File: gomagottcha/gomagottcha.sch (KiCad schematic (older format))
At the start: 88 parts, among them J1 USB_B_Micro, J2 Arduino_ICSP, SW1 SW_DIP_x01, U1 BM71BLES1FC2, U10 Buzzer_490-9647-1-ND, U11 IMU, U2 FT232RQ, U3 MCP7381, U4 ATMEGA1284P, U5 TPS2113APWR, U6 LCD_Tomagotcha, U7 MCP1700, U8 VMotor1670-1000-ND, U9 VMotor1670-1000-ND, Y1 Crystal

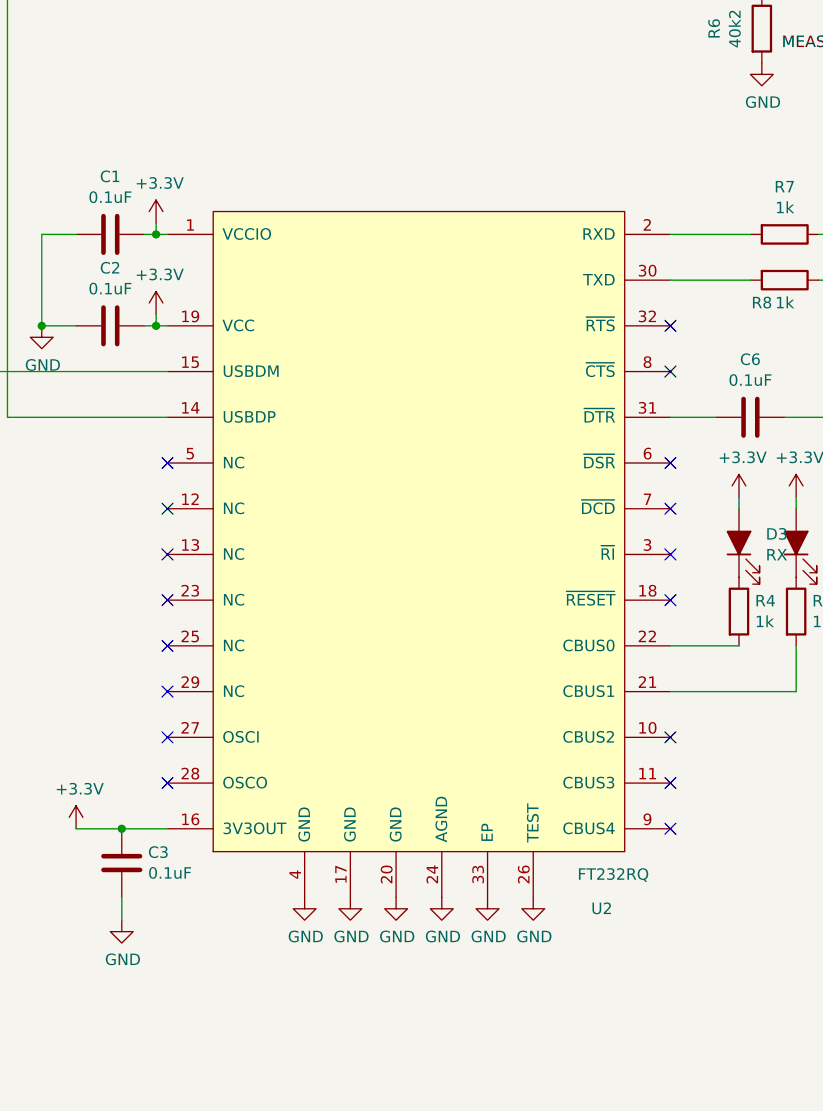
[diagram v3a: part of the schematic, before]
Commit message: Changed TCSP symbol from QFN to QFP
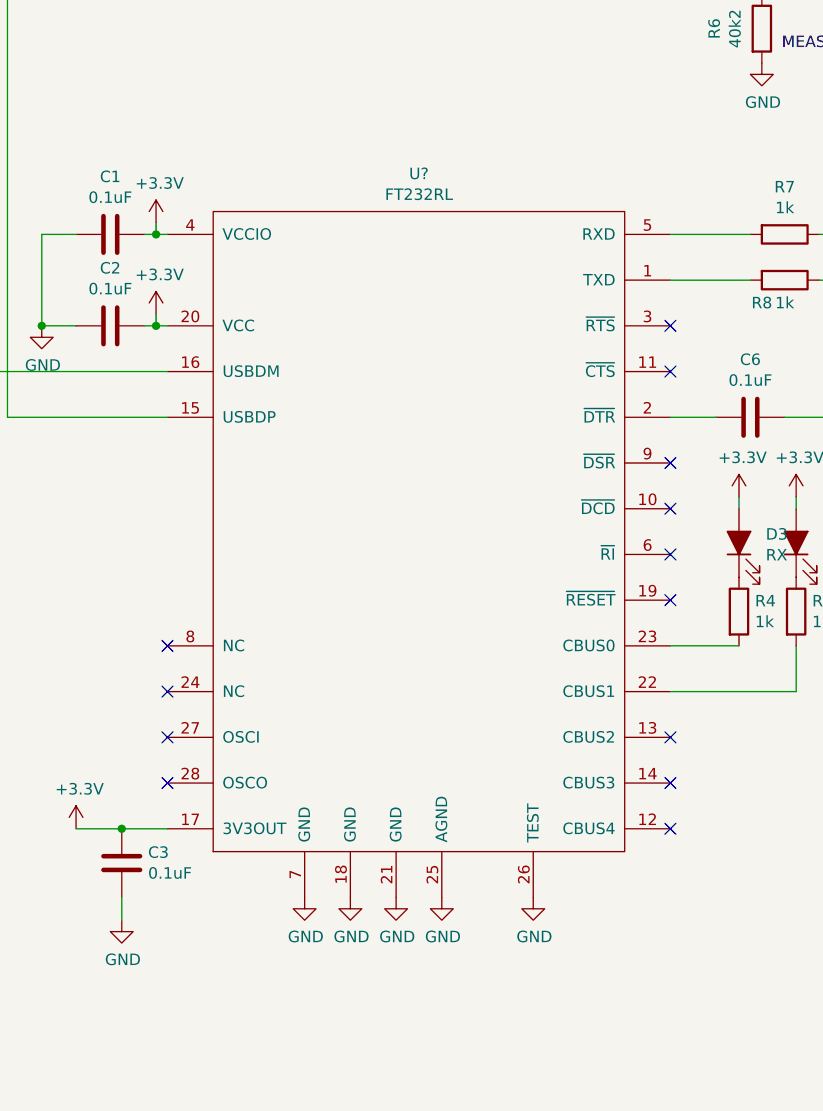
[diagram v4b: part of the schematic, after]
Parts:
- removed U2: FT232RQ, tama-footprints:QFN-32-1EP_5x5mm_P0.5mm_EP3.1x3.1mm_ThermalVias, symbol tama-sym:FT232RQ
- added U?: FT232RL, symbol tama-sym:FT232RL
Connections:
- net +3V3: now also U?.17 (3V3OUT), U?.20 (VCC), U?.4 (VCCIO)
- net GND: now also U?.18 (GND), U?.21 (GND), U?.25 (AGND), U?.26 (TEST), U?.7 (GND)
- net at J1.2 (D-): now also U?.16 (USBDM)
- net at J1.3 (D+): now also U?.15 (USBDP)
- net at R7.2: now also U?.5 (RXD)
- net at R9.2: now also U?.22 (CBUS1)
- net at R4.2: now also U?.23 (CBUS0)
- net at R8.2: now also U?.1 (TXD)
- net at C6.2: now also U?.2 (~DTR)
- no-connect marks 32 -> 28
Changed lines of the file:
@@
 	8200 1200 8200 1250
-$Comp
-L tama-sym:FT232RQ U2
-U 1 1 5CA563EE
-P 2750 5000
-F 0 "U2" H 3550 3350 50  0000 C CNN
-F 1 "FT232RQ" H 3600 3500 50  0000 C CNN
-F 2 "tama-footprints:QFN-32-1EP_5x5mm_P0.5mm_EP3.1x3.1mm_ThermalVias" H 2750 5950 50  0001 C CNN
-F 3 "" H 2750 5950 50  0001 C CNN
-	1    2750 5000
-	1    0    0    -1
-$EndComp
 $Comp
 L power:GND #PWR0106
@@
 	1100 4100 1250 4100
 Connection ~ 1100 4100
-NoConn ~ 1650 4700
-NoConn ~ 1650 4900
-NoConn ~ 1650 5100
-NoConn ~ 1650 5300
 NoConn ~ 1650 5500
 NoConn ~ 1650 5700
@@
 F 3 "" H 2850 6600 50  0001 C CNN
 	1    2850 6600
-	1    0    0    -1
-$EndComp
-$Comp
-L power:GND #PWR0116
-U 1 1 5CA6129E
-P 3050 6600
-F 0 "#PWR0116" H 3050 6350 50  0001 C CNN
-F 1 "GND" H 3055 6427 50  0000 C CNN
-F 2 "" H 3050 6600 50  0001 C CNN
-F 3 "" H 3050 6600 50  0001 C CNN
-	1    3050 6600
 	1    0    0    -1
 $EndComp
@@
 Wire Wire Line
 	3550 1300 3400 1300
+$Comp
+L tama-sym:FT232RL U?
+U 1 1 5CAFC7D3
+P 2750 5000
+F 0 "U?" H 2750 6565 50  0000 C CNN
+F 1 "FT232RL" H 2750 6474 50  0000 C CNN
+F 2 "" H 2750 5950 50  0001 C CNN
+F 3 "" H 2750 5950 50  0001 C CNN
+	1    2750 5000
+	1    0    0    -1
+$EndComp
 $EndSCHEMATC

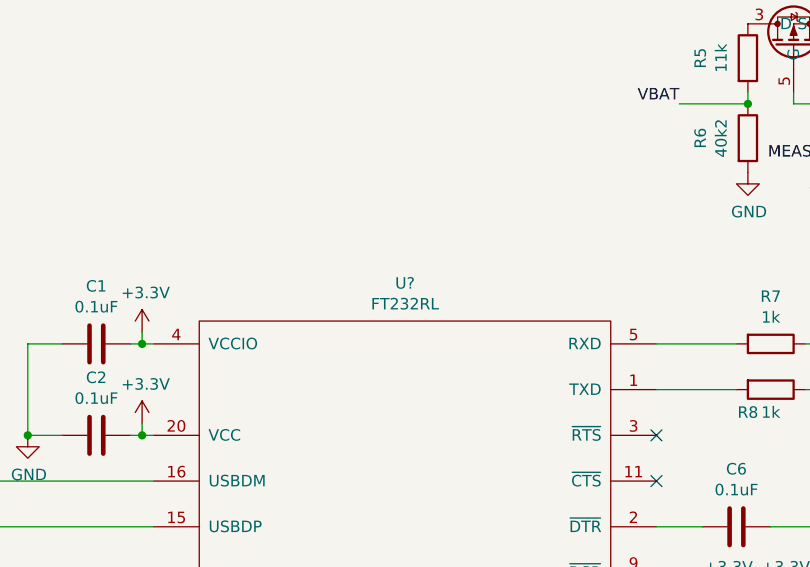
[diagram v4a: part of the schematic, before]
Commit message: Footprints are done, TODO: Layout
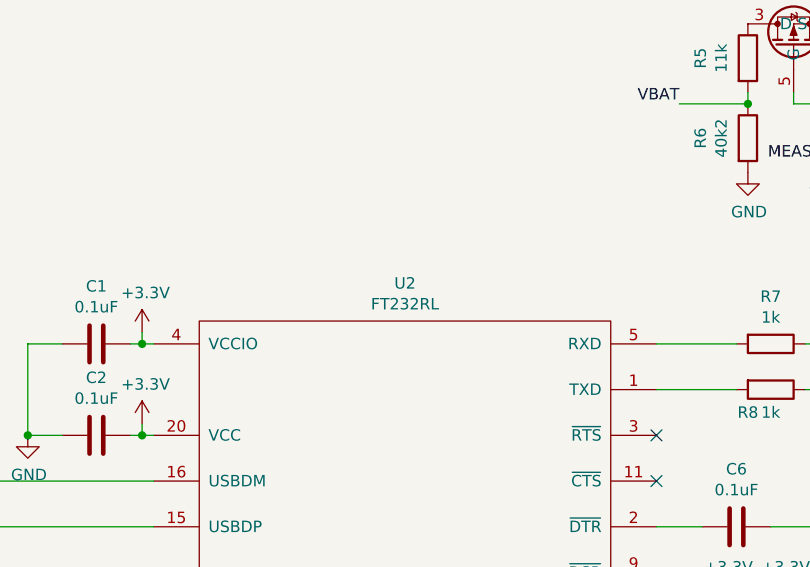
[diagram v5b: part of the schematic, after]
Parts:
- U2: renamed from U?; footprint (none) -> tama-footprints:SSOP-28_5.3x10.2mm_P0.65mm
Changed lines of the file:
@@
 	3550 1300 3400 1300
 $Comp
-L tama-sym:FT232RL U?
+L tama-sym:FT232RL U2
 U 1 1 5CAFC7D3
 P 2750 5000
-F 0 "U?" H 2750 6565 50  0000 C CNN
+F 0 "U2" H 2750 6565 50  0000 C CNN
 F 1 "FT232RL" H 2750 6474 50  0000 C CNN
-F 2 "" H 2750 5950 50  0001 C CNN
+F 2 "tama-footprints:SSOP-28_5.3x10.2mm_P0.65mm" H 2750 5950 50  0001 C CNN
 F 3 "" H 2750 5950 50  0001 C CNN
 	1    2750 5000

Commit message: started layout
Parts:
- added R26, R27: 10k, tama-footprints:R_0603_1608Metric, symbol Device:R
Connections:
- net +3V3: now also R26.2, R27.2
- net GND: now also C5.2
- net SCL: now also R27.1
- net SDA: now also R26.1
- net at D2.1 (K), R2.2: no longer C5.2
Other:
- moved on the sheet: C5
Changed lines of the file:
@@
 	0    -1   -1   0
 $EndComp
-Wire Wire Line
-	4000 8850 3750 8850
 Text Label 2750 9350 3    50   ~ 0
 RST_N
@@
 Text Notes 11750 1400 0    50   ~ 0
 Power Indicator
-$Comp
-L tama-sym:C C5
-U 1 1 5CAC3476
-P 3750 9000
-F 0 "C5" V 3800 9100 50  0000 C CNN
-F 1 "10uF" V 3900 9000 50  0000 C CNN
-F 2 "tama-footprints:C_0603_1608Metric" H 3788 8850 50  0001 C CNN
-F 3 "~" H 3750 9000 50  0001 C CNN
-	1    3750 9000
-	1    0    0    -1
-$EndComp
-Connection ~ 3750 8850
-Wire Wire Line
-	3750 8850 3650 8850
 Wire Wire Line
 	3750 9150 4000 9150
-Connection ~ 3750 9150
 Wire Wire Line
 	3350 9050 3350 9150
@@
 	1    0    0    -1
 $EndComp
+$Comp
+L tama-sym:C C5
+U 1 1 5CAC3476
+P 4400 9000
+F 0 "C5" V 4450 9100 50  0000 C CNN
+F 1 "10uF" V 4550 9000 50  0000 C CNN
+F 2 "tama-footprints:C_0603_1608Metric" H 4438 8850 50  0001 C CNN
+F 3 "~" H 4400 9000 50  0001 C CNN
+	1    4400 9000
+	1    0    0    -1
+$EndComp
+Wire Wire Line
+	4000 8850 4400 8850
+Wire Wire Line
+	3650 8850 4000 8850
+Connection ~ 4000 8850
+$Comp
+L power:GND #PWR0116
+U 1 1 5CB1BD55
+P 4400 9150
+F 0 "#PWR0116" H 4400 8900 50  0001 C CNN
+F 1 "GND" H 4405 8977 50  0000 C CNN
+F 2 "" H 4400 9150 50  0001 C CNN
+F 3 "" H 4400 9150 50  0001 C CNN
+	1    4400 9150
+	1    0    0    -1
+$EndComp
+$Comp
+L Device:R R26
+U 1 1 5CB2121E
+P 8950 6600
+F 0 "R26" V 8743 6600 50  0000 C CNN
+F 1 "10k" V 8834 6600 50  0000 C CNN
+F 2 "tama-footprints:R_0603_1608Metric" V 8880 6600 50  0001 C CNN
+F 3 "~" H 8950 6600 50  0001 C CNN
+	1    8950 6600
+	-1   0    0    1
+$EndComp
+$Comp
+L Device:R R27
+U 1 1 5CB2130E
+P 9250 6600
+F 0 "R27" V 9043 6600 50  0000 C CNN
+F 1 "10k" V 9134 6600 50  0000 C CNN
+F 2 "tama-footprints:R_0603_1608Metric" V 9180 6600 50  0001 C CNN
+F 3 "~" H 9250 6600 50  0001 C CNN
+	1    9250 6600
+	-1   0    0    1
+$EndComp
+$Comp
+L power:+3.3V #PWR0174
+U 1 1 5CB21570
+P 9250 6400
+F 0 "#PWR0174" H 9250 6250 50  0001 C CNN
+F 1 "+3.3V" H 9265 6573 50  0000 C CNN
+F 2 "" H 9250 6400 50  0001 C CNN
+F 3 "" H 9250 6400 50  0001 C CNN
+	1    9250 6400
+	1    0    0    -1
+$EndComp
+Wire Wire Line
+	9250 6400 9250 6450
+Wire Wire Line
+	9250 6450 8950 6450
+Connection ~ 9250 6450
+Wire Wire Line
+	8500 6750 8950 6750
+Wire Wire Line
+	8500 6850 9250 6850
+Wire Wire Line
+	9250 6850 9250 6750
 $EndSCHEMATC

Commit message: REVERT TO THIS IF REPINNING DOESNT WORK
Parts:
- BT1: footprint tama-footprints:battery_holder -> tama-footprints:PhoenixContact_MSTBVA_2,5_2-G_1x02_P5.00mm_Vertical
- U6: renamed from U5; footprint tama-footprints:VSON-8_3.1x3.1mm_P0.65mm -> tama-footprints:TSSOP-8_4.4x3mm_P0.65mm
- renumbered C6 to C5, C5 to C6, R26 to R19, R19 to R20, R20 to R21, R27 to R22, R21 to R23, R22 to R24, R23 to R25, R24 to R26, R25 to R27, U8 to U10, U?P3 to U11, U?N3 to U11, U9 to U12, U10 to U13, U11 to U14, U?N1 to U4, U?P1 to U4, U4 to U5, U?P2 to U7, U?N2 to U7, U6 to U8, U7 to U9

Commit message: TODO: Add screw holes and maybe picture
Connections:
- net A6 is gone; now on net WR: U5.31 ((ADC6/PCINT6)_PA6)
- net A7 is gone; now on net RD: U5.30 ((ADC7/PCINT7)_PA7)
- net SS is gone; now on net RX_IND: U5.44 ((~SS~/OC0B/PCINT12)_PB4)
- net BUTTON1: now also U5.35 ((ADC2/PCINT2)_PA2); no longer U5.15 (PD6_(PCINT30/OC2B/ICP))
- net BUTTON2: now also U5.36 ((ADC1/PCINT1)_PA1); no longer U5.26 (PC7_(TOSC2/PCINT23))
- net BUTTON3: now also U5.40 ((XCK0/T0/PCINT8)_PB0); no longer U5.36 ((ADC1/PCINT1)_PA1)
- net CS1: now also U5.34 ((ADC3/PCINT3)_PA3); no longer U5.22 (PC3_(PCINT19/TMS))
- net CTS: now also U5.41 ((T1/CLKO/PCINT9)_PB1); no longer U5.35 ((ADC2/PCINT2)_PA2)
- net PWM_1: now also U5.24 (PC5_(TDI/PCINT21)); no longer U5.13 (PD4_(PCINT28/XCK1/OC1B))
- net RD: no longer U5.21 (PC2_(PCINT18/TCK))
- net RST_N: now also U5.42 ((AIN0/INT2/PCINT10)_PB2); no longer U5.34 ((ADC3/PCINT3)_PA3)
- net RTS: now also U5.43 ((AIN1/OC0A/PCINT11)_PB3); no longer U5.33 ((ADC4/PCINT4)_PA4)
- net RX_IND: no longer U5.32 ((ADC5/PCINT5)_PA5)
- net WR: no longer U5.24 (PC5_(TDI/PCINT21))
- net PB0 renamed INT_XL
- net INT_XL: now also U5.21 (PC2_(PCINT18/TCK)); no longer U5.40 ((XCK0/T0/PCINT8)_PB0)
- net PB1 renamed DRDY_MAG
- net DRDY_MAG: now also U5.22 (PC3_(PCINT19/TMS)); no longer U5.41 ((T1/CLKO/PCINT9)_PB1)
- net PB2 renamed INT_MAG
- net INT_MAG: now also U5.15 (PD6_(PCINT30/OC2B/ICP)); no longer U5.42 ((AIN0/INT2/PCINT10)_PB2)
- net PB3 renamed A0
- net A0: now also U5.32 ((ADC5/PCINT5)_PA5); no longer U5.43 ((AIN1/OC0A/PCINT11)_PB3)
- net PC4 renamed RES
- net RES: now also U5.33 ((ADC4/PCINT4)_PA4); no longer U5.23 (PC4_(TDO/PCINT20))
- no-connect marks 28 -> 31
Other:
- moved on the sheet: C29, C30, C31
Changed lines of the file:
@@
 	1    0    0    -1
 $EndComp
-Text Label 8500 5800 0    50   ~ 0
-A6
-Text Label 8500 5900 0    50   ~ 0
-A7
 Text Label 8500 6750 0    50   ~ 0
 SDA
 Text Label 8500 6850 0    50   ~ 0
 SCL
-Text Label 8500 3700 0    50   ~ 0
-SS
 Text Label 8500 4650 0    50   ~ 0
 MOSI
@@
 L tama-sym:C C30
 U 1 1 5CAEB3C3
-P 13050 9350
-F 0 "C30" V 12798 9350 50  0000 C CNN
-F 1 "10uF" V 12900 9350 50  0000 C CNN
-F 2 "tama-footprints:C_0603_1608Metric" H 13088 9200 50  0001 C CNN
-F 3 "~" H 13050 9350 50  0001 C CNN
-	1    13050 9350
+P 13200 9350
+F 0 "C30" V 12948 9350 50  0000 C CNN
+F 1 "10uF" V 13050 9350 50  0000 C CNN
+F 2 "tama-footprints:C_0603_1608Metric" H 13238 9200 50  0001 C CNN
+F 3 "~" H 13200 9350 50  0001 C CNN
+	1    13200 9350
 	0    1    1    0
 $EndComp
@@
 L tama-sym:C C31
 U 1 1 5CAEB45B
-P 13050 9600
-F 0 "C31" V 12798 9600 50  0000 C CNN
-F 1 "100nF" V 13200 9600 50  0000 C CNN
-F 2 "tama-footprints:C_0603_1608Metric" H 13088 9450 50  0001 C CNN
-F 3 "~" H 13050 9600 50  0001 C CNN
-	1    13050 9600
+P 13200 9600
+F 0 "C31" V 12948 9600 50  0000 C CNN
+F 1 "100nF" V 13350 9600 50  0000 C CNN
+F 2 "tama-footprints:C_0603_1608Metric" H 13238 9450 50  0001 C CNN
+F 3 "~" H 13200 9600 50  0001 C CNN
+	1    13200 9600
 	0    1    1    0
 $EndComp
@@
 L power:GND #PWR074
 U 1 1 5CB0C516
-P 13200 9700
-F 0 "#PWR074" H 13200 9450 50  0001 C CNN
-F 1 "GND" H 13205 9527 50  0000 C CNN
-F 2 "" H 13200 9700 50  0001 C CNN
-F 3 "" H 13200 9700 50  0001 C CNN
-	1    13200 9700
+P 13350 9700
+F 0 "#PWR074" H 13350 9450 50  0001 C CNN
+F 1 "GND" H 13355 9527 50  0000 C CNN
+F 2 "" H 13350 9700 50  0001 C CNN
+F 3 "" H 13350 9700 50  0001 C CNN
+	1    13350 9700
 	1    0    0    -1
 $EndComp
@@
 L tama-sym:C C29
 U 1 1 5CB0C58F
-P 13050 9050
-F 0 "C29" V 12798 9050 50  0000 C CNN
-F 1 "100nF" V 12889 9050 50  0000 C CNN
-F 2 "tama-footprints:C_0603_1608Metric" H 13088 8900 50  0001 C CNN
-F 3 "~" H 13050 9050 50  0001 C CNN
-	1    13050 9050
-	0    1    1    0
-$EndComp
-Wire Wire Line
-	12600 9350 12900 9350
-Wire Wire Line
-	12900 9350 12900 9600
-Connection ~ 12900 9350
-Wire Wire Line
-	13200 9350 13200 9600
-Wire Wire Line
-	13200 9600 13200 9700
-Connection ~ 13200 9600
-Wire Wire Line
-	12600 9250 12900 9250
-Connection ~ 13200 9350
-Wire Wire Line
-	12900 9250 12900 9350
-Connection ~ 12900 9250
+P 13200 9050
+F 0 "C29" V 12948 9050 50  0000 C CNN
+F 1 "100nF" V 13039 9050 50  0000 C CNN
+F 2 "tama-footprints:C_0603_1608Metric" H 13238 8900 50  0001 C CNN
+F 3 "~" H 13200 9050 50  0001 C CNN
+	1    13200 9050
+	0    1    1    0
+$EndComp
+Wire Wire Line
+	13050 9350 13050 9600
+Connection ~ 13050 9350
+Wire Wire Line
+	13350 9350 13350 9600
+Wire Wire Line
+	13350 9600 13350 9700
+Connection ~ 13350 9600
+Connection ~ 13350 9350
+Wire Wire Line
+	13050 9250 13050 9350
+Connection ~ 13050 9250
 $Comp
 L power:+3.3V #PWR073
 U 1 1 5CB2EDD6
-P 12900 9000
-F 0 "#PWR073" H 12900 8850 50  0001 C CNN
-F 1 "+3.3V" H 12915 9173 50  0000 C CNN
-F 2 "" H 12900 9000 50  0001 C CNN
-F 3 "" H 12900 9000 50  0001 C CNN
-	1    12900 9000
-	1    0    0    -1
-$EndComp
-Connection ~ 12900 9050
-Wire Wire Line
-	12900 9050 12900 9000
-Wire Wire Line
-	12900 9050 12900 9250
-Wire Wire Line
-	13200 9050 13200 9350
-Text Label 8500 4100 0    50   ~ 0
-PB0
-Text Label 12600 9050 0    50   ~ 0
-PB0
-Text Label 8500 4000 0    50   ~ 0
-PB1
-Text Label 12600 9150 0    50   ~ 0
-PB1
-Text Label 8500 3900 0    50   ~ 0
-PB2
-Text Label 12600 9550 0    50   ~ 0
-PB2
+P 13050 9000
+F 0 "#PWR073" H 13050 8850 50  0001 C CNN
+F 1 "+3.3V" H 13065 9173 50  0000 C CNN
+F 2 "" H 13050 9000 50  0001 C CNN
+F 3 "" H 13050 9000 50  0001 C CNN
+	1    13050 9000
+	1    0    0    -1
+$EndComp
+Connection ~ 13050 9050
+Wire Wire Line
+	13050 9050 13050 9000
+Wire Wire Line
+	13050 9050 13050 9250
+Wire Wire Line
+	13350 9050 13350 9350
 $Comp
 L power:GND #PWR072
@@
 	1    0    0    -1
 $EndComp
-Text Label 8500 3800 0    50   ~ 0
-PB3
-Text Label 8600 9400 0    50   ~ 0
-PB3
 Text Label 8600 10400 0    50   ~ 0
 MOSI
@@
 	1    0    0    -1
 $EndComp
-Text Label 8500 6450 0    50   ~ 0
-PC4
-Text Label 8600 9300 0    50   ~ 0
-PC4
 Wire Wire Line
 	8600 9300 8950 9300
@@
 Text Label 3950 2650 2    50   ~ 0
 VBAT
-Text Label 8500 5200 0    50   ~ 0
-VBAT
 Text Label 4700 2900 2    50   ~ 0
 MEAS_BAT
@@
 Wire Wire Line
 	5750 2050 6650 2050
-Text Label 5850 7150 2    50   ~ 0
+Text Label 8500 6350 0    50   ~ 0
 PWM_1
 Text Label 5850 7250 2    50   ~ 0
@@
 Text Label 8600 9500 0    50   ~ 0
 WR
-Text Label 8500 6350 0    50   ~ 0
-WR
-Text Label 8500 6650 0    50   ~ 0
-RD
 Text Label 8600 9600 0    50   ~ 0
 RD
 Text Label 8600 9200 0    50   ~ 0
-CS1
-Text Label 8500 6550 0    50   ~ 0
 CS1
 Text Label 10750 4650 0    50   ~ 0
@@
 Text Label 12650 3500 1    50   ~ 0
 BUTTON3
-Text Label 5850 7350 2    50   ~ 0
-BUTTON1
-Text Label 8500 6150 0    50   ~ 0
-BUTTON2
-Text Label 8500 5300 0    50   ~ 0
-BUTTON3
 Text Label 2550 9350 3    50   ~ 0
 BLE_TX
@@
 Text Label 2650 9350 3    50   ~ 0
 RTS
-Text Label 8500 5400 0    50   ~ 0
-CTS
-Text Label 8500 5500 0    50   ~ 0
-RST_N
-Text Label 8500 5600 0    50   ~ 0
-RTS
-Text Label 8500 5700 0    50   ~ 0
-RX_IND
 $Comp
 L power:+3.3V #PWR067
@@
 Wire Wire Line
 	9250 6850 9250 6750
+Text Label 8600 9300 0    50   ~ 0
+RES
+Text Label 8600 9400 0    50   ~ 0
+A0
+Text Label 8500 5900 0    50   ~ 0
+RD
+Text Label 8500 5800 0    50   ~ 0
+WR
+Text Label 8500 5700 0    50   ~ 0
+A0
+Text Label 8500 5600 0    50   ~ 0
+RES
+Text Label 8500 5500 0    50   ~ 0
+CS1
+Text Label 8500 5200 0    50   ~ 0
+VBAT
+Text Label 8500 5400 0    50   ~ 0
+BUTTON1
+Text Label 8500 5300 0    50   ~ 0
+BUTTON2
+Text Label 8500 4100 0    50   ~ 0
+BUTTON3
+Text Label 12600 9050 0    50   ~ 0
+INT_XL
+Text Label 12600 9150 0    50   ~ 0
+DRDY_MAG
+Wire Wire Line
+	12600 9250 13050 9250
+Wire Wire Line
+	12600 9350 13050 9350
+Text Label 12600 9550 0    50   ~ 0
+INT_MAG
+Text Label 8500 6650 0    50   ~ 0
+INT_XL
+Text Label 8500 6550 0    50   ~ 0
+DRDY_MAG
+Text Label 5850 7350 2    50   ~ 0
+INT_MAG
+Text Label 8500 3700 0    50   ~ 0
+RX_IND
+Text Label 8500 3800 0    50   ~ 0
+RTS
+Text Label 8500 3900 0    50   ~ 0
+RST_N
+Text Label 8500 4000 0    50   ~ 0
+CTS
+NoConn ~ 8500 6450
+NoConn ~ 5850 7150
+NoConn ~ 8500 6150
 $EndSCHEMATC
